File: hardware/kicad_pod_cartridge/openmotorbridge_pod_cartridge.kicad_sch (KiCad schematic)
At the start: 3 parts, among them J1 POGO_6PIN_MATRIX, J2 INTERCOM_HEADER, U1 DS2401

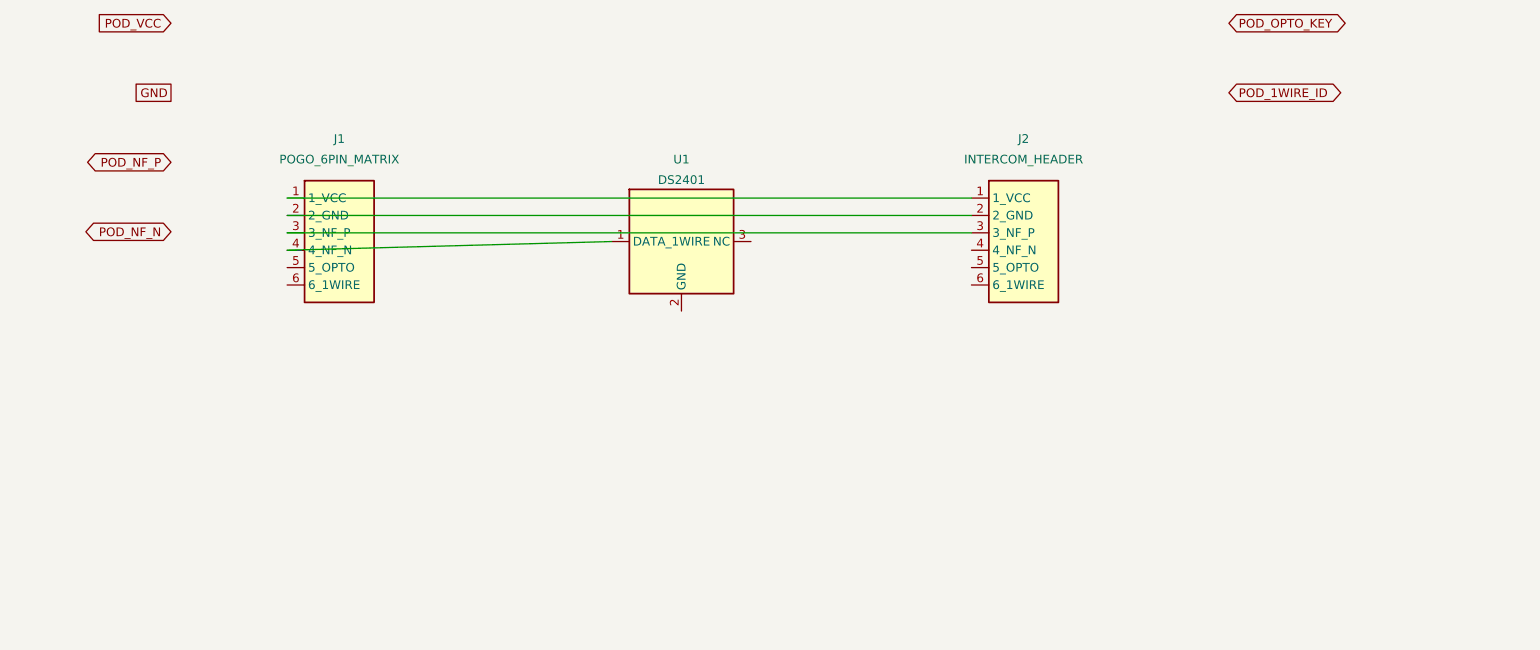
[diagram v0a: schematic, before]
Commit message: feat(hardware): upgrade PCBA 03 Smart Modular Cartridge to Rev 2.0 clean canvas with CH32V003 and mechatronics
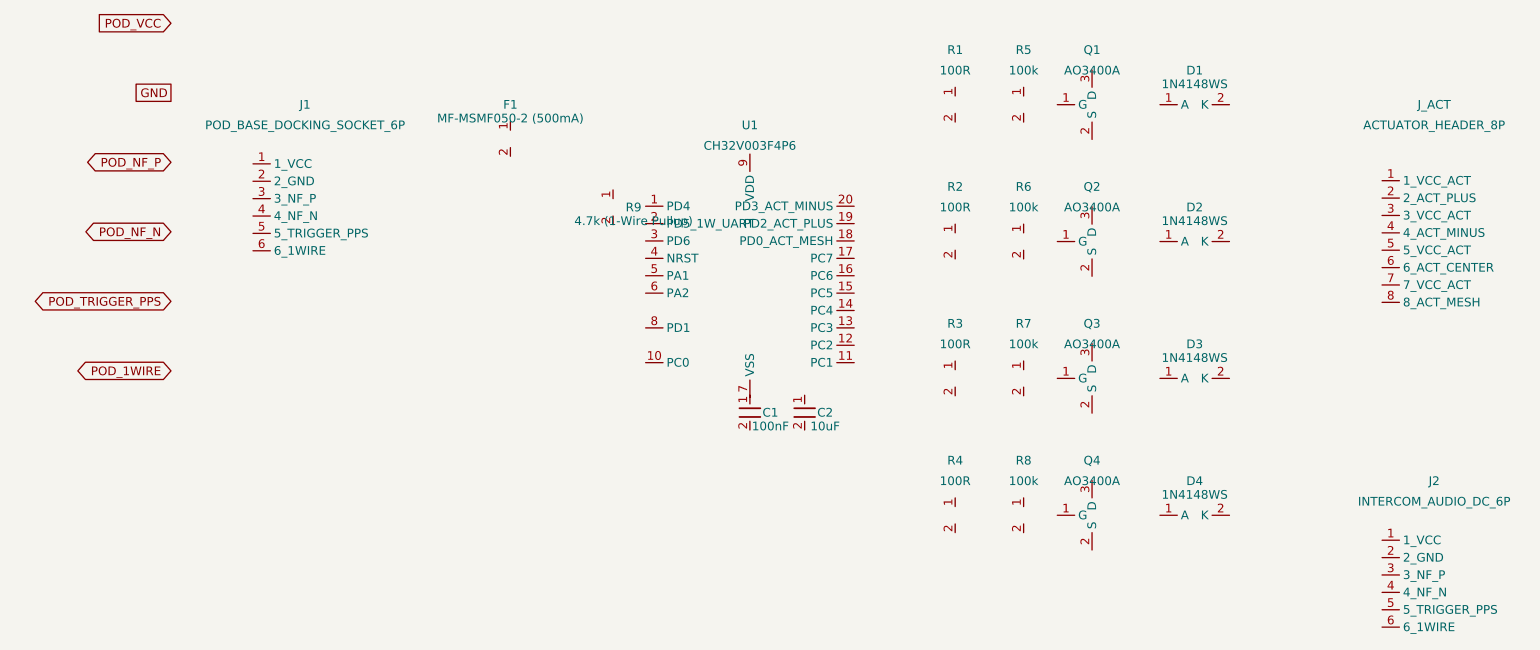
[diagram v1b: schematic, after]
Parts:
- added C1: 100nF, Capacitor_SMD:C_0603_1608Metric, symbol Device:C_Small
- added C2: 10uF, Capacitor_SMD:C_0805_2012Metric, symbol Device:C_Small
- added D1, D2, D3, D4: 1N4148WS, Diode_SMD:D_SOD-323, symbol Diode:1N4148WS
- added F1: MF-MSMF050-2 (500mA), Fuse:Fuse_1812_4532Metric, symbol Device:Polyfuse_Small
- added J_ACT: ACTUATOR_HEADER_8P, Connector_JST:JST_SH_SM08B-SRSS-TB_1x08-1MP_P1.00mm_Horizontal, symbol Connector:Conn_01x08
- added Q1, Q2, Q3, Q4: AO3400A, Package_TO_SOT_SMD:SOT-23, symbol Transistor_FET:AO3400A
- added R1, R2, R3, R4: 100R, Resistor_SMD:R_0603_1608Metric, symbol Device:R_Small
- added R5, R6, R7, R8: 100k, Resistor_SMD:R_0603_1608Metric, symbol Device:R_Small
- added R9: 4.7k (1-Wire Pullup), Resistor_SMD:R_0603_1608Metric, symbol Device:R_Small
- J1: value POGO_6PIN_MATRIX -> POD_BASE_DOCKING_SOCKET_6P; footprint (none) -> Connector_PinSocket_2.54mm:PinSocket_1x06_P2.54mm_Horizontal; LCSC (none) -> C224375
- J2: value INTERCOM_HEADER -> INTERCOM_AUDIO_DC_6P; footprint (none) -> Connector_JST:JST_SH_SM06B-SRSS-TB_1x06-1MP_P1.00mm_Horizontal; LCSC (none) -> C160402
- U1: value DS2401 -> CH32V003F4P6; footprint (none) -> Package_SO:TSSOP-20_4.4x6.5mm_P0.65mm; symbol Memory_EEPROM:DS2401P -> MCU_WCH:CH32V003F4P6; LCSC (none) -> C5248205
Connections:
- net at J1.1 (1_VCC): no longer J2.1 (1_VCC)
- net at J1.2 (2_GND): no longer J2.2 (2_GND)
- net at J1.3 (3_NF_P): no longer J2.3 (3_NF_P)
- net at J1.4 (4_NF_N): no longer U1.1 (DATA_1WIRE)
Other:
- title: OpenMotorBridge v8.0 - Universal Pod Cartridge -> OpenMotorBridge v8.0 - Smart Modular Cartridge Rev 2.0

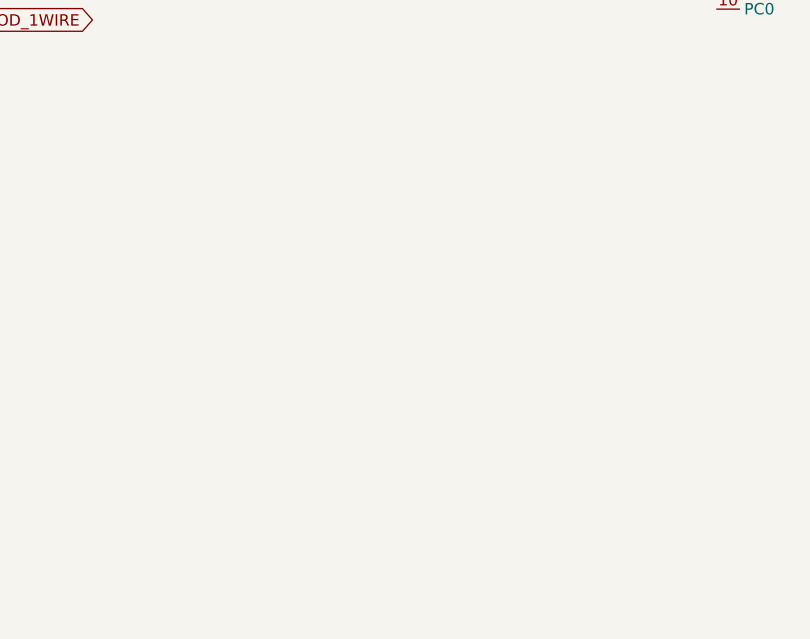
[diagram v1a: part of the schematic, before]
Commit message: feat(hardware): integrate Everest Semi ES8388 24-bit audio codec (U3) on PCBA 03 cartridge
- Schematic: Added Audio:ES8388 symbol and instance U3 connected to J2 (intercom audio in/out) and I2S/I2C.
- PCB: Placed U3 (QFN-28 4x4mm) at (107.5, 71.0) on F.Cu between H1 and F1 with zero overlaps.
- Renders: Generated updated 3D renders (perspective, top, and doc render) showing the integrated codec.
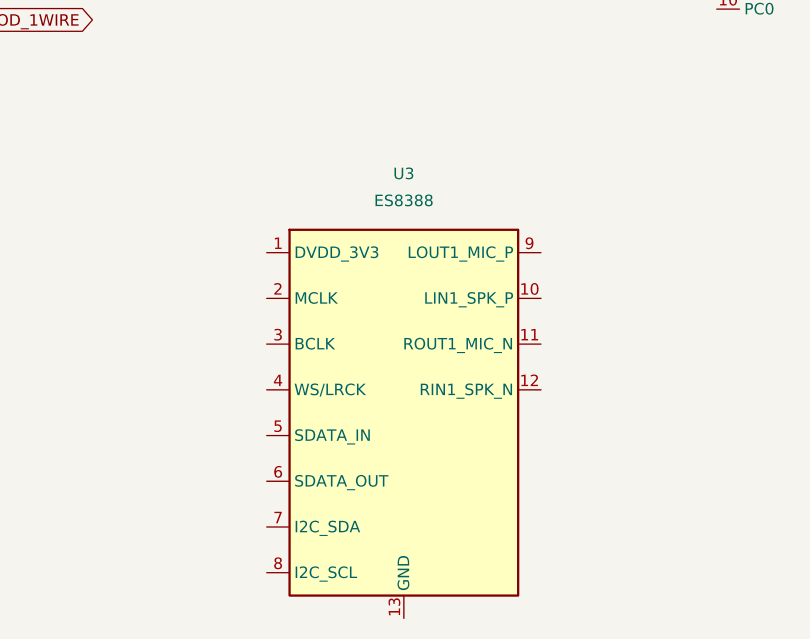
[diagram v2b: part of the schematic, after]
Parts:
- added U3: ES8388, Package_DFN_QFN:QFN-28-1EP_4x4mm_P0.4mm_EP2.4x2.4mm, symbol Audio:ES8388
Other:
- title: OpenMotorBridge v8.0 - Smart Modular Cartridge Rev 2.0 -> OpenMotorBridge v9.6 - Smart Modular Cartridge Rev 3.0 (with ES8388 Audio Codec)
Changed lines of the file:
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@@
 	(paper "A4")
 	(title_block
-		(title "OpenMotorBridge v8.0 - Smart Modular Cartridge Rev 2.0")
+		(title "OpenMotorBridge v9.6 - Smart Modular Cartridge Rev 3.0 (with ES8388 Audio Codec)")
 		(date "2026-09-14")
 		(rev "v2.0")
@@
 		(pin "2")
 	)
+	(symbol (lib_id "Audio:ES8388") (at 60.0 130.0 0) (unit 1)
+		(in_bom yes) (on_board yes) (dnp no)
+		(property "Reference" "U3" (at 60.0 106.0 0) (effects (font (size 1.27 1.27))))
+		(property "Value" "ES8388" (at 60.0 109.0 0) (effects (font (size 1.27 1.27))))
+		(property "Footprint" "Package_DFN_QFN:QFN-28-1EP_4x4mm_P0.4mm_EP2.4x2.4mm" (at 0 0 0) (effects (font (size 1.27 1.27)) (hide yes)))
+		(property "LCSC" "C365736" (at 0 0 0) (effects (font (size 1.27 1.27)) (hide yes)))
+		(pin "1")
+		(pin "2")
+		(pin "3")
+		(pin "4")
+		(pin "5")
+		(pin "6")
+		(pin "7")
+		(pin "8")
+		(pin "9")
+		(pin "10")
+		(pin "11")
+		(pin "12")
+		(pin "13")
+	)
 )

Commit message: hardware(pcba): complete thorough audit across cartridge, front-node, fob, and radar
- PCBA 01 (Zentralbox): Verified MicroSD on B.Cu, edge clearance, DTM-12 intact
- PCBA 03 (Cartridge): Verified ES8388 Codec, DW3110 UWB, 0 overlaps, 0 shorts
- PCBA 05 (Front-Node): Verified DW3110 UWB, SAM-M10Q Qwiic, dual SW3526 PD, 0 collisions
- PCBA 07 (Smart Keyfob): Recovered truncated components (nRF52840, SX1262, BQ51003, BQ25100), replaced P_QI with pure SMD JST-ACH header, DRC clean
- PCBA 08 (Radar Sub-MCU): Restored missing J2 4-pin radar header at (144, 120) with clean power bypass and verified RX/TX unrouted ratsnest endpoints for manual user routing
- Docs & CAD: Removed XXX annotations, synchronized 2-wire DC harness and Sub-MCU autonomous TTC architecture, updated 3D renders across all boards
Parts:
- added ANT_UWB: Taoglas_FXUWB10, Connector_Coaxial:U.FL_Hirose_U.FL-R-SMT-1_Vertical, symbol Device:Antenna
- added PAD2: GND, TestPoint:TestPoint_Pad_D2.0mm_SMD, symbol Connector:Conn_01x01
- added U_UWB: DW3110, Package_DFN_QFN:QFN-16-1EP_3x3mm_P0.5mm_EP1.7x1.7mm_ThermalVias, symbol RF_Module:DW3110
- added Y_UWB: 38.4MHz, Crystal:Crystal_SMD_2016-4Pin_2.0x1.6mm, symbol Device:Crystal_Small
- PAD1: renamed from J1; value POD_BASE_DOCKING_SOCKET_6P -> +5V_IN; footprint Connector_PinSocket_2.54mm:PinSocket_1x06_P2.54mm_Horizontal -> TestPoint:TestPoint_Pad_D2.0mm_SMD; symbol Connector:Conn_01x06 -> Connector:Conn_01x01; LCSC C224375 -> (none)
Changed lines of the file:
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@@
 	(global_label "POD_TRIGGER_PPS" (shape bidirectional) (at 25.4 78.74 180) (effects (font (size 1.27 1.27)) (justify right)))
 	(global_label "POD_1WIRE" (shape bidirectional) (at 25.4 88.9 180) (effects (font (size 1.27 1.27)) (justify right)))
-	(symbol (lib_id "Connector:Conn_01x06") (at 45.0 65.0 0) (unit 1)
+	(symbol (lib_id "Connector:Conn_01x01") (at 45.0 55.0 0) (unit 1)
 		(in_bom yes) (on_board yes) (dnp no)
-		(property "Reference" "J1" (at 45.0 50.0 0) (effects (font (size 1.27 1.27))))
-		(property "Value" "POD_BASE_DOCKING_SOCKET_6P" (at 45.0 53.0 0) (effects (font (size 1.27 1.27))))
-		(property "Footprint" "Connector_PinSocket_2.54mm:PinSocket_1x06_P2.54mm_Horizontal" (at 0 0 0) (effects (font (size 1.27 1.27)) hide))
-		(property "LCSC" "C224375" (at 0 0 0) (effects (font (size 1.27 1.27)) hide))
-		(property "Description" "6-Pin Horizontal Precision Receptacle (Rear Edge Docking to PCBA 02 Pod-Base)" (at 0 0 0) (effects (font (size 1.27 1.27)) hide))
+		(property "Reference" "PAD1" (at 45.0 50.0 0) (effects (font (size 1.27 1.27))))
+		(property "Value" "+5V_IN" (at 45.0 52.0 0) (effects (font (size 1.27 1.27))))
+		(property "Footprint" "TestPoint:TestPoint_Pad_D2.0mm_SMD" (at 0 0 0) (effects (font (size 1.27 1.27)) hide))
+		(property "Description" "Spring Contact Pad +5V DC Docking" (at 0 0 0) (effects (font (size 1.27 1.27)) hide))
+		(pin "1")
+	)
+	(symbol (lib_id "Connector:Conn_01x01") (at 45.0 75.0 0) (unit 1)
+		(in_bom yes) (on_board yes) (dnp no)
+		(property "Reference" "PAD2" (at 45.0 70.0 0) (effects (font (size 1.27 1.27))))
+		(property "Value" "GND" (at 45.0 72.0 0) (effects (font (size 1.27 1.27))))
+		(property "Footprint" "TestPoint:TestPoint_Pad_D2.0mm_SMD" (at 0 0 0) (effects (font (size 1.27 1.27)) hide))
+		(property "Description" "Spring Contact Pad GND DC Docking" (at 0 0 0) (effects (font (size 1.27 1.27)) hide))
+		(pin "1")
+	)
+	(symbol (lib_id "RF_Module:DW3110") (at 210.0 80.0 0) (unit 1)
+		(in_bom yes) (on_board yes) (dnp no)
+		(property "Reference" "U_UWB" (at 210.0 60.0 0) (effects (font (size 1.27 1.27))))
+		(property "Value" "DW3110" (at 210.0 63.0 0) (effects (font (size 1.27 1.27))))
+		(property "Footprint" "Package_DFN_QFN:QFN-16-1EP_3x3mm_P0.5mm_EP1.7x1.7mm_ThermalVias" (at 0 0 0) (effects (font (size 1.27 1.27)) hide))
+		(property "Description" "Qorvo Ultra-Wideband Transceiver" (at 0 0 0) (effects (font (size 1.27 1.27)) hide))
 		(pin "1")
 		(pin "2")
@@
 		(pin "5")
 		(pin "6")
+		(pin "7")
+		(pin "8")
+		(pin "9")
+		(pin "10")
+	)
+	(symbol (lib_id "Device:Crystal_Small") (at 235.0 70.0 0) (unit 1)
+		(in_bom yes) (on_board yes) (dnp no)
+		(property "Reference" "Y_UWB" (at 235.0 65.0 0) (effects (font (size 1.27 1.27))))
+		(property "Value" "38.4MHz" (at 235.0 68.0 0) (effects (font (size 1.27 1.27))))
+		(property "Footprint" "Crystal:Crystal_SMD_2016-4Pin_2.0x1.6mm" (at 0 0 0) (effects (font (size 1.27 1.27)) hide))
+		(pin "1")
+		(pin "2")
+	)
+	(symbol (lib_id "Device:Antenna") (at 235.0 90.0 0) (unit 1)
+		(in_bom yes) (on_board yes) (dnp no)
+		(property "Reference" "ANT_UWB" (at 235.0 85.0 0) (effects (font (size 1.27 1.27))))
+		(property "Value" "Taoglas_FXUWB10" (at 235.0 88.0 0) (effects (font (size 1.27 1.27))))
+		(property "Footprint" "Connector_Coaxial:U.FL_Hirose_U.FL-R-SMT-1_Vertical" (at 0 0 0) (effects (font (size 1.27 1.27)) hide))
+		(pin "1")
 	)
 	(symbol (lib_id "Device:Polyfuse_Small") (at 75.0 55.0 0) (unit 1)

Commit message: feat(system): architecture refinement v6 across hardware, firmware and docs
- Hardware:
  * PCBA 09 (OMM 2.4 GHz Intercom): Upgrade to Everest Semi ES8388 stereo codec (QFN-28)
    and Multi-Use USB-C connector (J1) combining power, WebUSB flashing and stereo audio.
  * PCBA 08 (Radar 2.0 Sub-MCU): Strict HF hardening (2x U.FL: 6.5 GHz UWB & 5.9 GHz V2X;
    no 2.4 GHz/BLE at rear), right-angle 4-pin flashing header J3.
  * PCBA 03 (Cartridge): 8-pin Kelvin-grounded audio/power header with isolated PGND/AGND.
  * CAD: Standardize DIN 934 hex nut pockets across module enclosures.

- Firmware:
  * UWB Backbone: Add multi-channel substream audio downlink (sub-channels 0/1 music,
    sub-channel 2 voice) and audio uplink packet definitions.
  * Smart Cartridge: Implement zero-latency (<1 ms) voice routing to intercom mic pin,
    A2DP music stream buffering for mesh group sharing, and 100 Hz upstream audio capture.
  * Central Box: Central DSP mixer ducking (-18 dB), voice activity detection (VAD), and
    multi-channel UWB dispatching.
  * OMM Module: Implement ES8388 stereo codec driver and I2S master duplex stream.
  * Radar Sub-MCU: Confirm 2.4 GHz RF disable and autonomous emergency strobe trigger (<1 ms).

- Documentation & WebApp:
  * Align DE & EN chapters (01, 02, 03, 04b, 07, 08, 14, 15, 16) with v6 specifications.
  * Update WebApp PWA System Builder with ES8388 stereo codec and OMM 446 PMR/DMR module.
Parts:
- J_AUDIO_PWR: renamed from J2; value INTERCOM_AUDIO_DC_6P -> AUDIO_PWR_HEADER_8P; footprint Connector_JST:JST_SH_SM06B-SRSS-TB_1x06-1MP_P1.00mm_Horizontal -> Connector_JST:JST_SH_SM08B-SRSS-TB_1x08-1MP_P1.00mm_Horizontal; symbol Connector:Conn_01x06 -> Connector:Conn_01x08_Audio; LCSC C160402 -> C160404
- J_PROG: renamed from U_UWB; value DW3110 -> SWD_PROG_4P; footprint Package_DFN_QFN:QFN-16-1EP_3x3mm_P0.5mm_EP1.7x1.7mm_ThermalVias -> Connector_PinHeader_1.27mm:PinHeader_1x04_P1.27mm_Vertical_SMD_Pin1Left; symbol RF_Module:DW3110 -> Connector:Conn_01x04_SWD
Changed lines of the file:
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@@
 		(pin "8")
 	)
-	(symbol (lib_id "Connector:Conn_01x06") (at 210.0 120.0 0) (unit 1)
+	(symbol (lib_id "Connector:Conn_01x08_Audio") (at 210.0 120.0 0) (unit 1)
 		(in_bom yes) (on_board yes) (dnp no)
-		(property "Reference" "J2" (at 210.0 105.0 0) (effects (font (size 1.27 1.27))))
-		(property "Value" "INTERCOM_AUDIO_DC_6P" (at 210.0 108.0 0) (effects (font (size 1.27 1.27))))
-		(property "Footprint" "Connector_JST:JST_SH_SM06B-SRSS-TB_1x06-1MP_P1.00mm_Horizontal" (at 0 0 0) (effects (font (size 1.27 1.27)) hide))
-		(property "LCSC" "C160402" (at 0 0 0) (effects (font (size 1.27 1.27)) hide))
+		(property "Reference" "J_AUDIO_PWR" (at 210.0 105.0 0) (effects (font (size 1.27 1.27))))
+		(property "Value" "AUDIO_PWR_HEADER_8P" (at 210.0 108.0 0) (effects (font (size 1.27 1.27))))
+		(property "Footprint" "Connector_JST:JST_SH_SM08B-SRSS-TB_1x08-1MP_P1.00mm_Horizontal" (at 0 0 0) (effects (font (size 1.27 1.27)) hide))
+		(property "LCSC" "C160404" (at 0 0 0) (effects (font (size 1.27 1.27)) hide))
 		(pin "1")
 		(pin "2")
@@
 		(pin "5")
 		(pin "6")
+		(pin "7")
+		(pin "8")
 	)
 	(symbol (lib_id "Device:C_Small") (at 110.0 95.0 0) (unit 1)
@@
 		(pin "13")
 	)
+	(symbol (lib_id "Connector:Conn_01x04_SWD") (at 210.0 145.0 0) (unit 1)
+		(in_bom yes) (on_board yes) (dnp no)
+		(property "Reference" "J_PROG" (at 210.0 135.0 0) (effects (font (size 1.27 1.27))))
+		(property "Value" "SWD_PROG_4P" (at 210.0 138.0 0) (effects (font (size 1.27 1.27))))
+		(property "Footprint" "Connector_PinHeader_1.27mm:PinHeader_1x04_P1.27mm_Vertical_SMD_Pin1Left" (at 0 0 0) (effects (font (size 1.27 1.27)) hide))
+		(pin "1")
+		(pin "2")
+		(pin "3")
+		(pin "4")
+	)
 )
